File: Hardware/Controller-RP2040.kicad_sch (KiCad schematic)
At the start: 43 parts, among them J1 Conn_01x07_Male, J2 Conn_01x04_Male, J3 Conn_01x02_Male, J4 Conn_01x02_Male, J5 Conn_01x02_Male, J6 Conn_01x02_Male, J7 Conn_01x08_Male, J8 QWIIC_Vertical, J9 QWIIC_Stackable, Q1 DMG1012T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

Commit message: Bit more of the RP2040...
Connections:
- net DEV_GPIO is gone; now on net io14: J7.7 (Pin_7)
- net io11 is gone; now on net MOSI: U1.14 (GPIO11)
- net io12 is gone; now on net MISO: U1.15 (GPIO12)
- net io13 is gone; now on net SCLK: U1.16 (GPIO13)
- net ~{SCS} is gone; now on net MOSI: J7.8 (Pin_8)
- net MISO: now also J7.6 (Pin_6); no longer J7.4 (Pin_4)
- net MOSI: no longer J7.6 (Pin_6)
- net SCL: no longer J7.3 (Pin_3)
- net SCLK: now also J7.4 (Pin_4); no longer J7.2 (Pin_2)
- net SDA: no longer J7.5 (Pin_5)
- net DEV_RST renamed ~{RESET}
- new net RESET: J7.2 (Pin_2)
- new net ~{SCS}1: J7.5 (Pin_5)
- new net ~{SCS}2: J7.3 (Pin_3)

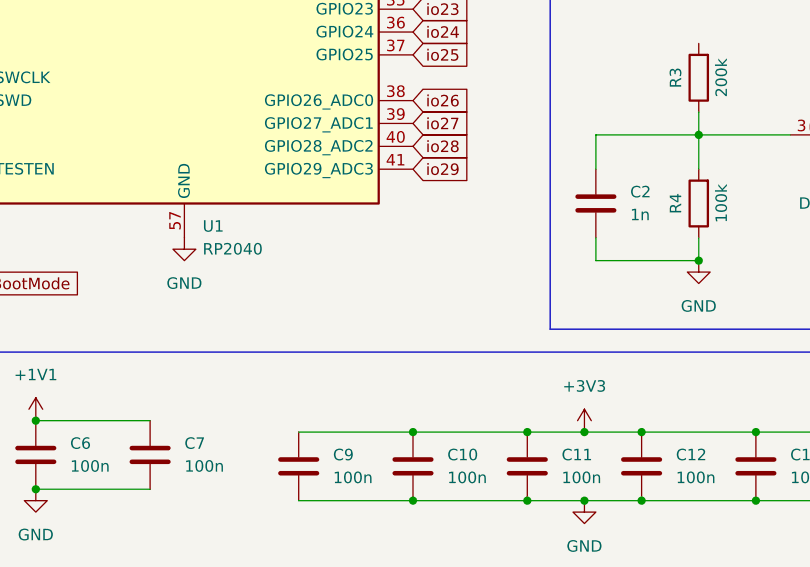
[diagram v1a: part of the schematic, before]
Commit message: I2C on the RP2040
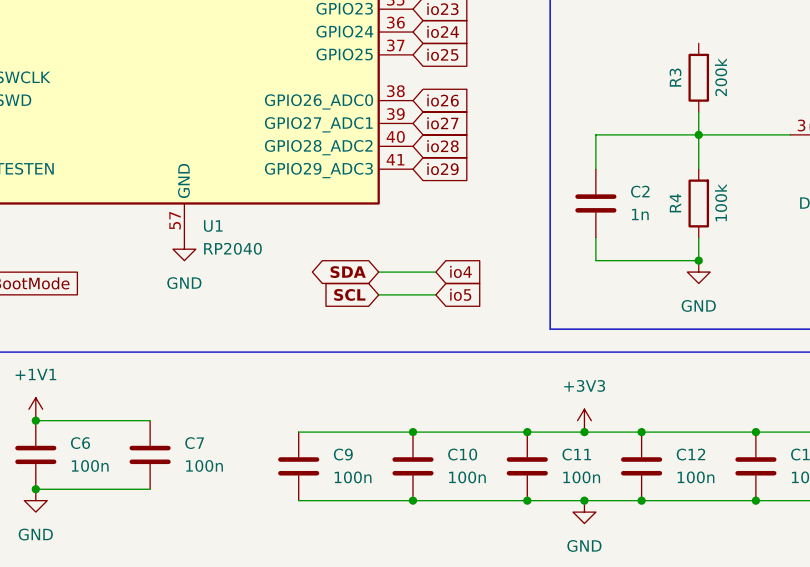
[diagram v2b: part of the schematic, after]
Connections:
- net io4 is gone; now on net SDA: U1.6 (GPIO4)
- net io5 is gone; now on net SCL: U1.7 (GPIO5)
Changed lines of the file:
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@@
+    (stroke (width 0) (type default) (color 0 0 0 0))
+  )
+  (wire (pts (xy 220.98 133.35) (xy 227.33 133.35))
     (stroke (width 0) (type default) (color 0 0 0 0))
   )
@@
   )
   (wire (pts (xy 110.49 87.63) (xy 110.49 83.82))
+    (stroke (width 0) (type default) (color 0 0 0 0))
+  )
+  (wire (pts (xy 220.98 135.89) (xy 227.33 135.89))
     (stroke (width 0) (type default) (color 0 0 0 0))
   )
@@
     )
   )
+  (global_label "io5" (shape input) (at 227.33 135.89 0) (fields_autoplaced)
+    (effects (font (size 1.27 1.27)) (justify left))
+    (property "Intersheet References" "${INTERSHEET_REFS}" (id 0) (at 232.7064 135.8106 0)
+      (effects (font (size 1.27 1.27)) (justify left) hide)
+    )
+  )
   (global_label "SCLK" (shape bidirectional) (at 120.65 46.99 180) (fields_autoplaced)
     (effects (font (size 1.27 1.27)) (justify right))
@@
     )
   )
+  (global_label "SDA" (shape bidirectional) (at 220.98 133.35 180) (fields_autoplaced)
+    (effects (font (size 1.27 1.27) bold) (justify right))
+    (property "Intersheet References" "${INTERSHEET_REFS}" (id 0) (at 214.8084 133.223 0)
+      (effects (font (size 1.27 1.27) bold) (justify right) hide)
+    )
+  )
   (global_label "io18" (shape input) (at 224.79 91.44 0) (fields_autoplaced)
     (effects (font (size 1.27 1.27)) (justify left))
@@
     )
   )
+  (global_label "io4" (shape input) (at 227.33 133.35 0) (fields_autoplaced)
+    (effects (font (size 1.27 1.27)) (justify left))
+    (property "Intersheet References" "${INTERSHEET_REFS}" (id 0) (at 232.7064 133.2706 0)
+      (effects (font (size 1.27 1.27)) (justify left) hide)
+    )
+  )
   (global_label "io21" (shape input) (at 224.79 99.06 0) (fields_autoplaced)
     (effects (font (size 1.27 1.27)) (justify left))
@@
     )
   )
+  (global_label "SCL" (shape input) (at 220.98 135.89 180) (fields_autoplaced)
+    (effects (font (size 1.27 1.27) (thickness 0.254) bold) (justify right))
+    (property "Intersheet References" "${INTERSHEET_REFS}" (id 0) (at 214.8689 135.763 0)
+      (effects (font (size 1.27 1.27) (thickness 0.254) bold) (justify right) hide)
+    )
+  )

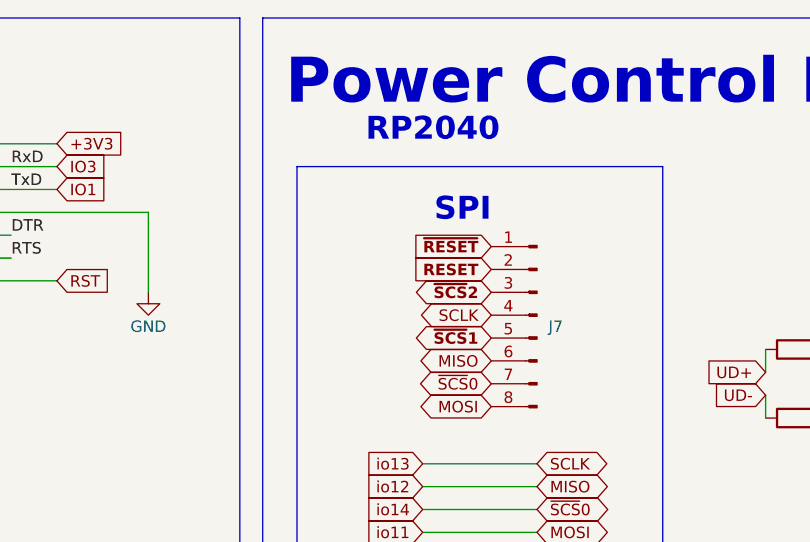
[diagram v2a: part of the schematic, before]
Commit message: Working on Controller-Tarduino Clone
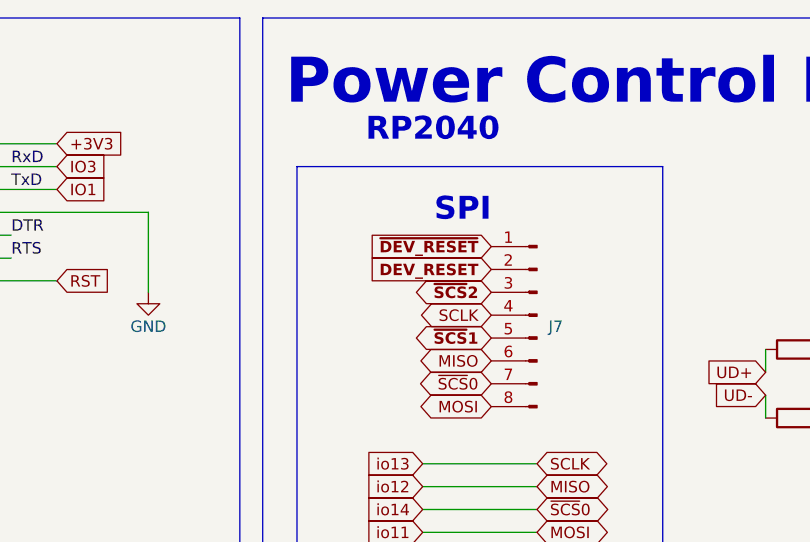
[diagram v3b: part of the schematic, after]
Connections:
- net RESET renamed DEV_RESET
- net ~{RESET} renamed ~{DEV_RESET}
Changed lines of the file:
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@@
     )
   )
-  (global_label "~{RESET}" (shape input) (at 120.65 39.37 180) (fields_autoplaced)
-    (effects (font (size 1.27 1.27) (thickness 0.254) bold) (justify right))
-    (property "Intersheet References" "${INTERSHEET_REFS}" (id 0) (at 112.3013 39.243 0)
+  (global_label "DEV_RESET" (shape input) (at 120.65 41.91 180) (fields_autoplaced)
+    (effects (font (size 1.27 1.27) (thickness 0.254) bold) (justify right))
+    (property "Intersheet References" "${INTERSHEET_REFS}" (id 0) (at 107.826 41.783 0)
       (effects (font (size 1.27 1.27) (thickness 0.254) bold) (justify right) hide)
     )
@@
     )
   )
-  (global_label "RESET" (shape input) (at 120.65 41.91 180) (fields_autoplaced)
-    (effects (font (size 1.27 1.27) (thickness 0.254) bold) (justify right))
-    (property "Intersheet References" "${INTERSHEET_REFS}" (id 0) (at 112.3013 41.783 0)
-      (effects (font (size 1.27 1.27) (thickness 0.254) bold) (justify right) hide)
-    )
-  )
   (global_label "io9" (shape input) (at 224.79 68.58 0) (fields_autoplaced)
     (effects (font (size 1.27 1.27)) (justify left))
@@
     )
   )
+  (global_label "~{DEV_RESET}" (shape input) (at 120.65 39.37 180) (fields_autoplaced)
+    (effects (font (size 1.27 1.27) (thickness 0.254) bold) (justify right))
+    (property "Intersheet References" "${INTERSHEET_REFS}" (id 0) (at 107.826 39.243 0)
+      (effects (font (size 1.27 1.27) (thickness 0.254) bold) (justify right) hide)
+    )
+  )

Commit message: Working on the RP2040 & cleaning up stuff...
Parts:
- added SW1, SW2: SW_Push, Tinker:SW_Push_TS273014TP, symbol Switch:SW_Push
- J9: value QWIIC_Stackable -> QWIIC_Stack_II
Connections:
- net BootMode: now also SW2.2
- net GND: now also U2.9 (EP), SW1.1, SW2.1; no longer Y1.2
- net Reset: now also SW1.2
- net Xin: no longer C1.1, U1.20 (XIN), Y1.1
- new net: C1.1, U1.20 (XIN), Y1.1
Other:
- note added: "I2C"
- note removed: "Footprint(s) only"
- moved on the sheet: C1, C15, C16, C2, C3, C4, C5, C8, J1, J2, J3, J4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
